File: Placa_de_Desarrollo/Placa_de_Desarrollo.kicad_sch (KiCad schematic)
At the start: 47 parts, among them J10 5V_OUT, J11 3.3V_OUT, J12 ADC_VREF, J13 GND, J14 AGND, J15 VSYS_ALIMEANTACION_EXTERNA, J16 3V3_EN, J17 DEVICE I2C0, J18 PINES GPIO, J19 ADC1, J2 USB_B_Micro, J20 ADC2, J21 ADC0, J3 DEVICE I2C0, J4 GND, J5 GND, J6 GND, J7 GND, J8 GND, J9 GND, SW1 RESET, SW2 RESET, U1 Pico, U2 LM317_TO-220

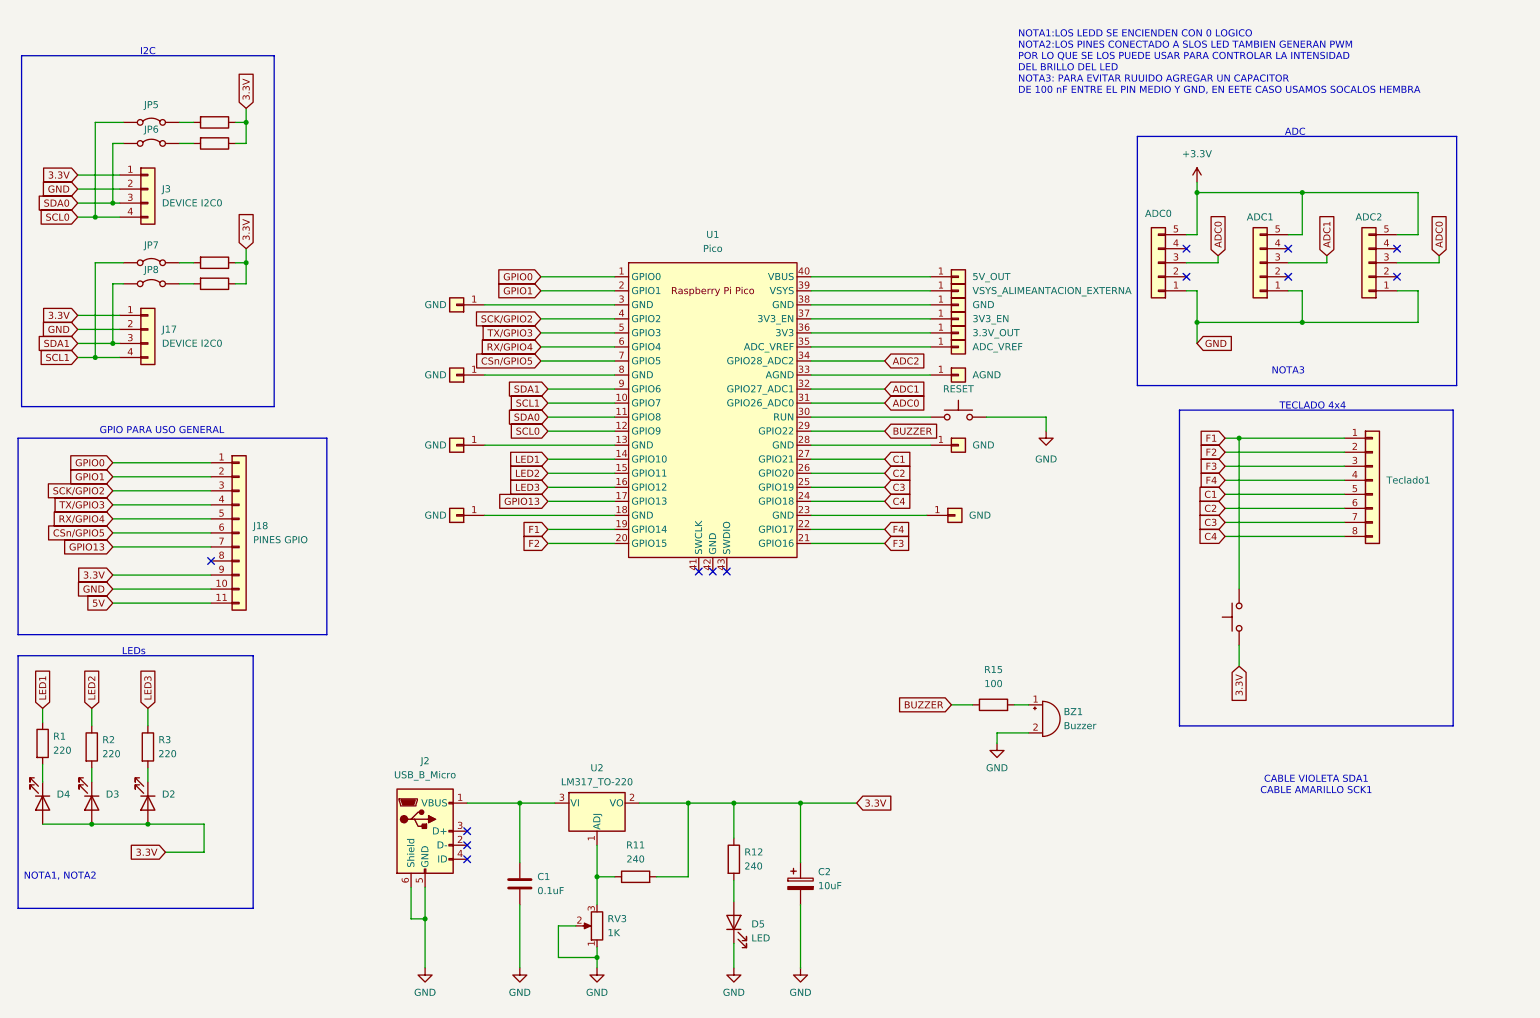
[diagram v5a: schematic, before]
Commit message: Actualizacion de Placa de Desarrollo, modificacionde pines
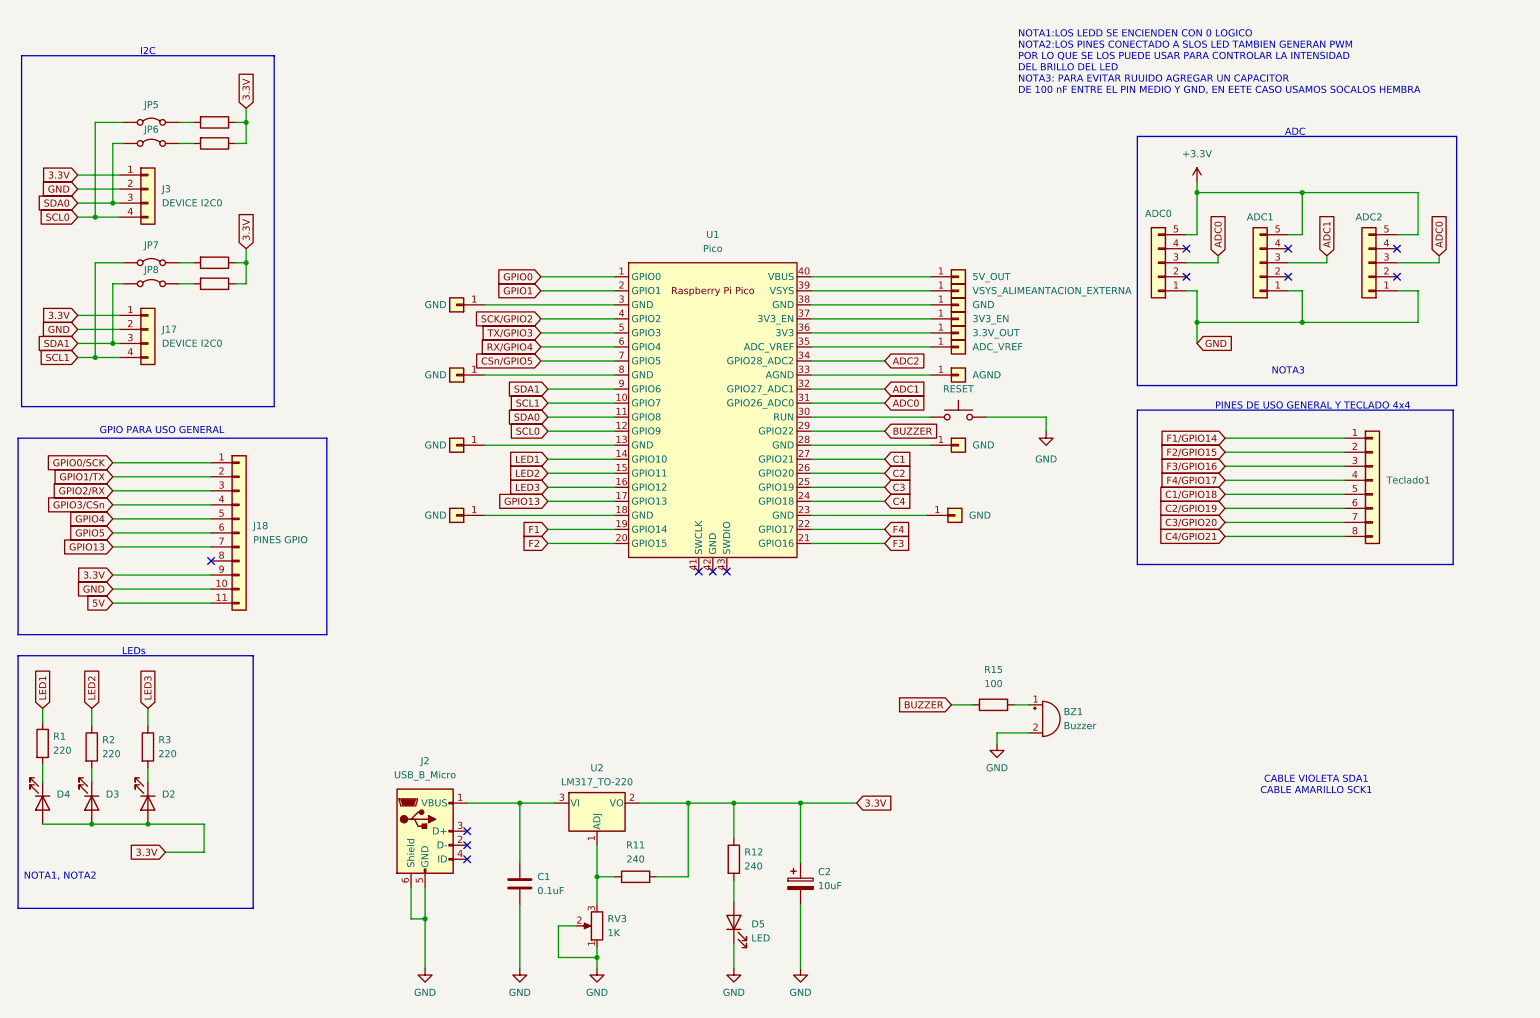
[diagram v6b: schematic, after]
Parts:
- removed SW2: RESET, symbol Switch:SW_Push
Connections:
- net C1: no longer Teclado1.5 (Pin_5)
- net C2: no longer Teclado1.6 (Pin_6)
- net C3: no longer Teclado1.7 (Pin_7)
- net C4: no longer Teclado1.8 (Pin_8)
- net CSn/GPIO5: no longer J18.6 (Pin_6)
- net F1: no longer Teclado1.1 (Pin_1)
- net F2: no longer Teclado1.2 (Pin_2)
- net F3: no longer Teclado1.3 (Pin_3)
- net F4: no longer Teclado1.4 (Pin_4)
- net GPIO0: no longer J18.1 (Pin_1)
- net GPIO1: no longer J18.2 (Pin_2)
- net RX/GPIO4: no longer J18.5 (Pin_5)
- net SCK/GPIO2: no longer J18.3 (Pin_3)
- net TX/GPIO3: no longer J18.4 (Pin_4)
- new net C1/GPIO18: Teclado1.5 (Pin_5)
- new net C2/GPIO19: Teclado1.6 (Pin_6)
- new net C3/GPIO20: Teclado1.7 (Pin_7)
- new net C4/GPIO21: Teclado1.8 (Pin_8)
- new net F1/GPIO14: Teclado1.1 (Pin_1)
- new net F2/GPIO15: Teclado1.2 (Pin_2)
- new net F3/GPIO16: Teclado1.3 (Pin_3)
- new net F4/GPIO17: Teclado1.4 (Pin_4)
- new net GPIO0/SCK: J18.1 (Pin_1)
- new net GPIO1/TX: J18.2 (Pin_2)
- new net GPIO2/RX: J18.3 (Pin_3)
- new net GPIO3/CSn: J18.4 (Pin_4)
- new net GPIO4: J18.5 (Pin_5)
- new net GPIO5: J18.6 (Pin_6)
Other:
- note added: "PINES DE USO GENERAL Y TECLADO 4x4"
- note removed: "TECLADO 4x4"
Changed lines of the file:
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@@
 	)
 	(junction
-		(at 238.76 90.17)
-		(diameter 0)
-		(color 0 0 0 0)
-	)
-	(junction
 		(at 41.275 160.02)
 		(diameter 0)
@@
 	(wire
 		(pts
-			(xy 238.76 127.635) (xy 238.76 131.445)
-		)
-		(stroke
-			(width 0)
-			(type default)
-		)
-	)
-	(wire
-		(pts
 			(xy 31.115 149.86) (xy 31.115 152.4)
 		)
@@
 	(wire
 		(pts
-			(xy 238.76 90.17) (xy 257.81 90.17)
+			(xy 236.22 90.17) (xy 257.81 90.17)
 		)
 		(stroke
@@
 	(wire
 		(pts
-			(xy 236.22 90.17) (xy 238.76 90.17)
-		)
-		(stroke
-			(width 0)
-			(type default)
-		)
-	)
-	(wire
-		(pts
 			(xy 44.45 165.1) (xy 51.435 165.1)
 		)
@@
 	(wire
 		(pts
-			(xy 238.76 90.17) (xy 238.76 117.475)
-		)
-		(stroke
-			(width 0)
-			(type default)
-		)
-	)
-	(wire
-		(pts
 			(xy 36.83 33.02) (xy 31.75 33.02)
 		)
@@
 	)
 	(rectangle
-		(start 227.965 85.09)
-		(end 277.495 142.24)
+		(start 220.345 85.09)
+		(end 277.495 113.03)
 		(stroke
 			(width 0)
@@
 		)
 	)
-	(text "TECLADO 4x4\n"
+	(text "PINES DE USO GENERAL Y TECLADO 4x4\n"
 		(exclude_from_sim no)
 		(at 252.095 84.455 0)
@@
 		)
 	)
-	(global_label "C1"
+	(global_label "C1{slash}GPIO18"
 		(shape input)
 		(at 236.22 100.33 180)
@@
 		)
 		(property "Intersheetrefs" "${INTERSHEET_REFS}"
-			(at 230.7553 100.33 0)
+			(at 222.5305 100.33 0)
 			(effects
 				(font
@@
 		)
 	)
-	(global_label "SCK{slash}GPIO2"
+	(global_label "GPIO2{slash}RX"
 		(shape input)
 		(at 34.925 99.695 180)
@@
 		)
 		(property "Intersheetrefs" "${INTERSHEET_REFS}"
-			(at 21.175 99.695 0)
+			(at 22.445 99.695 0)
 			(effects
 				(font
@@
 		)
 	)
-	(global_label "CSn{slash}GPIO5"
+	(global_label "GPIO5"
 		(shape input)
 		(at 34.925 107.315 180)
@@
 		)
 		(property "Intersheetrefs" "${INTERSHEET_REFS}"
-			(at 21.296 107.315 0)
+			(at 26.255 107.315 0)
 			(effects
 				(font
@@
 		)
 	)
-	(global_label "F4"
+	(global_label "F4{slash}GPIO17"
 		(shape input)
 		(at 236.22 97.79 180)
@@
 		)
 		(property "Intersheetrefs" "${INTERSHEET_REFS}"
-			(at 230.9367 97.79 0)
+			(at 222.7119 97.79 0)
 			(effects
 				(font
@@
 		)
 	)
-	(global_label "3.3V"
-		(shape input)
-		(at 238.76 131.445 270)
-		(fields_autoplaced yes)
-		(effects
-			(font
-				(size 1.27 1.27)
-			)
-			(justify right)
-		)
-		(property "Intersheetrefs" "${INTERSHEET_REFS}"
-			(at 238.76 138.5426 90)
-			(effects
-				(font
-					(size 1.27 1.27)
-				)
-				(justify right)
-				(hide yes)
-			)
-		)
-	)
 	(global_label "LED2"
 		(shape input)
@@
 		)
 	)
-	(global_label "GPIO1"
+	(global_label "GPIO1{slash}TX"
 		(shape input)
 		(at 34.925 97.155 180)
@@
 		)
 		(property "Intersheetrefs" "${INTERSHEET_REFS}"
-			(at 26.255 97.155 0)
+			(at 22.7474 97.155 0)
 			(effects
 				(font
@@
 		)
 	)
-	(global_label "RX{slash}GPIO4"
+	(global_label "GPIO4"
 		(shape input)
 		(at 34.925 104.775 180)
@@
 		)
 		(property "Intersheetrefs" "${INTERSHEET_REFS}"
-			(at 22.445 104.775 0)
+			(at 26.255 104.775 0)
 			(effects
 				(font
@@
 		)
 	)
-	(global_label "F1"
+	(global_label "F1{slash}GPIO14"
 		(shape input)
 		(at 236.22 90.17 180)
@@
 		)
 		(property "Intersheetrefs" "${INTERSHEET_REFS}"
-			(at 230.9367 90.17 0)
+			(at 222.7119 90.17 0)
 			(effects
 				(font
@@
 		)
 	)
-	(global_label "C2"
+	(global_label "C2{slash}GPIO19"
 		(shape input)
 		(at 236.22 102.87 180)
@@
 		)
 		(property "Intersheetrefs" "${INTERSHEET_REFS}"
-			(at 230.7553 102.87 0)
+			(at 222.5305 102.87 0)
 			(effects
 				(font
@@
 		)
 	)
-	(global_label "C3"
+	(global_label "C3{slash}GPIO20"
 		(shape input)
 		(at 236.22 105.41 180)
@@
 		)
 		(property "Intersheetrefs" "${INTERSHEET_REFS}"
-			(at 230.7553 105.41 0)
+			(at 222.5305 105.41 0)
 			(effects
 				(font
@@
 		)
 	)
-	(global_label "C4"
+	(global_label "C4{slash}GPIO21"
 		(shape input)
 		(at 236.22 107.95 180)
@@
 		)
 		(property "Intersheetrefs" "${INTERSHEET_REFS}"
-			(at 230.7553 107.95 0)
+			(at 222.5305 107.95 0)
 			(effects
 				(font
@@
 		)
 	)
-	(global_label "TX{slash}GPIO3"
+	(global_label "GPIO3{slash}CSn"
 		(shape input)
 		(at 34.925 102.235 180)
@@
 		)
 		(property "Intersheetrefs" "${INTERSHEET_REFS}"
-			(at 22.7474 102.235 0)
+			(at 21.296 102.235 0)
 			(effects
 				(font
@@
 		)
 	)
-	(global_label "F3"
+	(global_label "F3{slash}GPIO16"
 		(shape input)
 		(at 236.22 95.25 180)
@@
 		)
 		(property "Intersheetrefs" "${INTERSHEET_REFS}"
-			(at 230.9367 95.25 0)
+			(at 222.7119 95.25 0)
 			(effects
 				(font
@@
 		)
 	)
-	(global_label "F2"
+	(global_label "F2{slash}GPIO15"
 		(shape input)
 		(at 236.22 92.71 180)
@@
 		)
 		(property "Intersheetrefs" "${INTERSHEET_REFS}"
-			(at 230.9367 92.71 0)
+			(at 222.7119 92.71 0)
 			(effects
 				(font
@@
 		)
 	)
-	(global_label "GPIO0"
+	(global_label "GPIO0{slash}SCK"
 		(shape input)
 		(at 34.925 94.615 180)
@@
 		)
 		(property "Intersheetrefs" "${INTERSHEET_REFS}"
-			(at 26.255 94.615 0)
+			(at 21.175 94.615 0)
 			(effects
 				(font
@@
 					(unit 1)
 				)
-			)
-		)
-	)
-	(symbol
-		(lib_id "Switch:SW_Push")
-		(at 238.76 122.555 90)
-		(unit 1)
-		(exclude_from_sim no)
-		(in_bom yes)
-		(on_board yes)
-		(dnp no)
-		(fields_autoplaced yes)
-		(property "Reference" "SW2"
-			(at 231.14 122.555 0)
-			(effects
-				(font
-					(size 1.27 1.27)
-				)
-				(hide yes)
-			)
-		)
-		(property "Value" "RESET"
-			(at 240.665 122.5549 90)
-			(effects
-				(font
-					(size 1.27 1.27)
-				)
-				(justify right)
-				(hide yes)
-			)
-		)
-		(property "Footprint" ""
-			(at 233.68 122.555 0)
-			(effects
-				(font
-					(size 1.27 1.27)
-				)
-				(hide yes)
-			)
-		)
-		(property "Datasheet" "~"
-			(at 233.68 122.555 0)
-			(effects
-				(font
-					(size 1.27 1.27)
-				)
-				(hide yes)
-			)
-		)
-		(property "Description" "Push button switch, generic, two pins"
-			(at 238.76 122.555 0)
-			(effects
-				(font
-					(size 1.27 1.27)
-				)
-				(hide yes)
-			)
-		)
-		(pin "1"
-		)
-		(pin "2"
-		)
-		(instances
-			(project "Placa_de_Desarrollo"
-				(path "/fcc0771d-888f-40a3-a42c-2cc7ec6c456b"
-					(reference "SW2")
-					(unit 1)
-				)

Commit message: Actualizacion de placa de prueba
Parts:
- removed J10: 5V_OUT, symbol Connector_Generic:Conn_01x01
- removed J11: 3.3V_OUT, symbol Connector_Generic:Conn_01x01
- removed J12: ADC_VREF, symbol Connector_Generic:Conn_01x01
- removed J13, J4, J5, J6, J7, J8, J9: GND, symbol Connector_Generic:Conn_01x01
- removed J14: AGND, symbol Connector_Generic:Conn_01x01
- removed J15: VSYS_ALIMEANTACION_EXTERNA, symbol Connector_Generic:Conn_01x01
- removed J16: 3V3_EN, symbol Connector_Generic:Conn_01x01
- renumbered D4 to D1, D3 to D2, D2 to D3, D5 to D4, J3 to J1, J21 to J18, J17 to J2, J18 to J3, J2 to J4, JP5 to JP1, JP6 to JP2, JP7 to JP3, JP8 to JP4, R15 to R10, R9 to R4, R10 to R5, R13 to R6, R14 to R7, R11 to R8, R12 to R9, RV3 to RV1, U2 to U1, U1 to U2
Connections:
- net +3.3V is gone; now on net 3.3V: J18.5 (Pin_5), J19.5 (Pin_5), J20.5 (Pin_5)
- net C1 is gone; now on net C4/GPIO21: U2.27 (GPIO21)
- net C2 is gone; now on net C3/GPIO20: U2.26 (GPIO20)
- net C3 is gone; now on net C2/GPIO19: U2.25 (GPIO19)
- net C4 is gone; now on net C1/GPIO18: U2.24 (GPIO18)
- net CSn/GPIO5 is gone; now on net GPIO5: U2.7 (GPIO5)
- net F1 is gone; now on net F1/GPIO14: U2.19 (GPIO14)
- net F2 is gone; now on net F2/GPIO15: U2.20 (GPIO15)
- net F3 is gone; now on net F3/GPIO16: U2.21 (GPIO16)
- net F4 is gone; now on net F4/GPIO17: U2.22 (GPIO17)
- net GPIO0 is gone; now on net GPIO0/SCK: U2.1 (GPIO0)
- net GPIO1 is gone; now on net GPIO1/TX: U2.2 (GPIO1)
- net RX/GPIO4 is gone; now on net GPIO4: U2.6 (GPIO4)
- net SCK/GPIO2 is gone; now on net GPIO2/RX: U2.4 (GPIO2)
- net TX/GPIO3 is gone; now on net GPIO3/CSn: U2.5 (GPIO3)
- net 3.3V: now also JP1.1 (A), JP3.1 (A)
- net 5V: now also C1.1, J4.1 (VBUS), U1.3 (VI), U2.39 (VSYS)
- net ADC0: no longer J18.3 (Pin_3)
- net ADC2: now also J18.3 (Pin_3)
- net GND: now also JP2.1 (A), JP4.1 (A), U2.28 (GND), U2.38 (GND)
- net SCL0: no longer JP1.1 (A)
- net SCL1: no longer JP3.1 (A)
- net SDA0: no longer JP2.1 (A)
- net SDA1: no longer JP4.1 (A)
- no-connect marks 13 -> 23
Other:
- note added: "ALIMENTACION DE 5V POR MICRO USB"
- note added: "CONVERSOR ANALOGICO - DIGITAL"
- note added: "LEDS"
- note added: "PUERTOS I2C"
- note added: "TECLADO Y GPIO GENERAL"
- note removed: "ADC"
- note removed: "I2C"
- note removed: "LEDs"
- note removed: "PINES DE USO GENERAL Y TECLADO 4x4"
- moved on the sheet: BZ1, C1, C2, D1, D2, D3, D4, J1, J2, J3, J4, R1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

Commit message: Actualizacion de respo Kicad
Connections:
- net 3.3V: no longer JP1.1 (A), JP3.1 (A)
- net GND: no longer JP2.1 (A), JP4.1 (A)
- net SCL0: now also JP2.1 (A)
- net SCL1: now also JP3.1 (A)
- net SDA0: now also JP1.1 (A)
- net SDA1: now also JP4.1 (A)
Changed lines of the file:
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@@
-	)
-	(junction
-		(at 34.29 41.91)
-		(diameter 0)
-		(color 0 0 0 0)
 	)
 	(junction
@@
 	)
 	(junction
+		(at 35.56 49.53)
+		(diameter 0)
+		(color 0 0 0 0)
+	)
+	(junction
 		(at 45.72 154.94)
 		(diameter 0)
@@
 	)
 	(junction
+		(at 34.29 46.99)
+		(diameter 0)
+		(color 0 0 0 0)
+	)
+	(junction
 		(at 60.96 33.02)
 		(diameter 0)
@@
 	)
 	(junction
-		(at 35.56 44.45)
-		(diameter 0)
-		(color 0 0 0 0)
-	)
-	(junction
 		(at 59.69 168.91)
 		(diameter 0)
@@
 	)
 	(junction
-		(at 35.56 69.85)
-		(diameter 0)
-		(color 0 0 0 0)
-	)
-	(junction
-		(at 34.29 67.31)
+		(at 34.29 74.93)
 		(diameter 0)
 		(color 0 0 0 0)
@@
 		(color 0 0 0 0)
 	)
+	(junction
+		(at 35.56 72.39)
+		(diameter 0)
+		(color 0 0 0 0)
+	)
 	(no_connect
 		(at 36.83 160.02)
@@
 	(wire
 		(pts
-			(xy 34.29 58.42) (xy 34.29 67.31)
-		)
-		(stroke
-			(width 0)
-			(type default)
-		)
-	)
-	(wire
-		(pts
 			(xy 162.56 100.33) (xy 175.26 100.33)
 		)
@@
 	(wire
 		(pts
+			(xy 34.29 58.42) (xy 34.29 74.93)
+		)
+		(stroke
+			(width 0)
+			(type default)
+		)
+	)
+	(wire
+		(pts
 			(xy 137.16 173.99) (xy 156.21 173.99)
 		)
@@
 	(wire
 		(pts
+			(xy 34.29 74.93) (xy 45.72 74.93)
+		)
+		(stroke
+			(width 0)
+			(type default)
+		)
+	)
+	(wire
+		(pts
 			(xy 267.97 63.5) (xy 269.24 63.5)
 		)
@@
 	(wire
 		(pts
-			(xy 29.21 41.91) (xy 34.29 41.91)
-		)
-		(stroke
-			(width 0)
-			(type default)
-		)
-	)
-	(wire
-		(pts
 			(xy 115.57 74.93) (xy 127 74.93)
 		)
@@
 	(wire
 		(pts
-			(xy 34.29 33.02) (xy 34.29 41.91)
-		)
-		(stroke
-			(width 0)
-			(type default)
-		)
-	)
-	(wire
-		(pts
 			(xy 248.92 63.5) (xy 252.73 63.5)
 		)
@@
 	(wire
 		(pts
-			(xy 29.21 49.53) (xy 45.72 49.53)
+			(xy 29.21 49.53) (xy 35.56 49.53)
 		)
 		(stroke
@@
 	(wire
 		(pts
-			(xy 29.21 44.45) (xy 35.56 44.45)
-		)
-		(stroke
-			(width 0)
-			(type default)
-		)
-	)
-	(wire
-		(pts
 			(xy 60.96 36.83) (xy 60.96 33.02)
 		)
@@
 	(wire
 		(pts
-			(xy 35.56 36.83) (xy 35.56 44.45)
-		)
-		(stroke
-			(width 0)
-			(type default)
-		)
-	)
-	(wire
-		(pts
 			(xy 275.59 58.42) (xy 267.97 58.42)
 		)
@@
 	(wire
 		(pts
+			(xy 35.56 72.39) (xy 45.72 72.39)
+		)
+		(stroke
+			(width 0)
+			(type default)
+		)
+	)
+	(wire
+		(pts
 			(xy 275.59 57.15) (xy 275.59 58.42)
 		)
@@
 	(wire
 		(pts
-			(xy 29.21 69.85) (xy 35.56 69.85)
-		)
-		(stroke
-			(width 0)
-			(type default)
-		)
-	)
-	(wire
-		(pts
 			(xy 76.2 168.91) (xy 76.2 154.94)
 		)
@@
 	(wire
 		(pts
-			(xy 34.29 41.91) (xy 45.72 41.91)
+			(xy 29.21 41.91) (xy 45.72 41.91)
 		)
 		(stroke
@@
 	(wire
 		(pts
+			(xy 35.56 36.83) (xy 35.56 49.53)
+		)
+		(stroke
+			(width 0)
+			(type default)
+		)
+	)
+	(wire
+		(pts
 			(xy 52.07 115.57) (xy 52.07 118.11)
 		)
@@
 	(wire
 		(pts
-			(xy 35.56 69.85) (xy 45.72 69.85)
+			(xy 29.21 69.85) (xy 45.72 69.85)
 		)
 		(stroke
@@
 	(wire
 		(pts
+			(xy 34.29 46.99) (xy 45.72 46.99)
+		)
+		(stroke
+			(width 0)
+			(type default)
+		)
+	)
+	(wire
+		(pts
 			(xy 46.99 58.42) (xy 49.53 58.42)
 		)
@@
 	(wire
 		(pts
+			(xy 35.56 62.23) (xy 35.56 72.39)
+		)
+		(stroke
+			(width 0)
+			(type default)
+		)
+	)
+	(wire
+		(pts
 			(xy 252.73 63.5) (xy 252.73 69.85)
 		)
@@
 	(wire
 		(pts
+			(xy 34.29 33.02) (xy 34.29 46.99)
+		)
+		(stroke
+			(width 0)
+			(type default)
+		)
+	)
+	(wire
+		(pts
 			(xy 97.79 154.94) (xy 85.09 154.94)
 		)
@@
 	(wire
 		(pts
+			(xy 35.56 49.53) (xy 45.72 49.53)
+		)
+		(stroke
+			(width 0)
+			(type default)
+		)
+	)
+	(wire
+		(pts
 			(xy 115.57 67.31) (xy 127 67.31)
 		)
@@
 	(wire
 		(pts
-			(xy 29.21 67.31) (xy 34.29 67.31)
+			(xy 29.21 67.31) (xy 45.72 67.31)
 		)
 		(stroke
@@
 	(wire
 		(pts
-			(xy 29.21 74.93) (xy 45.72 74.93)
-		)
-		(stroke
-			(width 0)
-			(type default)
-		)
-	)
-	(wire
-		(pts
-			(xy 35.56 62.23) (xy 35.56 69.85)
+			(xy 29.21 74.93) (xy 34.29 74.93)
 		)
 		(stroke
@@
 	(wire
 		(pts
-			(xy 34.29 67.31) (xy 45.72 67.31)
-		)
-		(stroke
-			(width 0)
-			(type default)
-		)
-	)
-	(wire
-		(pts
 			(xy 52.07 105.41) (xy 52.07 107.95)
 		)
@@
 	(wire
 		(pts
-			(xy 29.21 72.39) (xy 45.72 72.39)
+			(xy 29.21 72.39) (xy 35.56 72.39)
 		)
 		(stroke
@@
 	(wire
 		(pts
-			(xy 29.21 46.99) (xy 45.72 46.99)
+			(xy 29.21 46.99) (xy 34.29 46.99)
 		)
 		(stroke
@@
 	(wire
 		(pts
-			(xy 35.56 44.45) (xy 45.72 44.45)
-		)
-		(stroke
+			(xy 29.21 44.45) (xy 45.72 44.45)
+		)
+		(stroke
